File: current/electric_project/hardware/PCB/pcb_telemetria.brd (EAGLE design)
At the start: 106.8 x 113.8 mm, 42 parts

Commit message: Schematic e code conforming
The mux pins in the code are now updated (EN on the ground rsrs) and the circuit project are already routed with the new mux pins
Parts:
- moved SUPPLY 6.87 mm to (96.6, 77.9)
- moved SHUNTS 6.60 mm to (96.3, 96.6)
- moved TEMP2 6.13 mm to (96.3, 85.4)
- moved TEMP1 5.98 mm to (96.4, 90.9)
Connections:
- removed net GND1: U$1.GND1
- net 13: now also HC4067.J2.6
- net 14: now also HC4067.J2.5
- net 33: no longer HC4067.J2.3
- net 34: no longer HC4067.J2.6
- net 35: no longer HC4067.J2.5
- net GND: now also HC4067.J2.3, U$1.GND1
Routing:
- net 14: track 0.00 -> 130.9 mm
- net 33: track 118.8 -> 0.00 mm
- net 13: track 0.00 -> 114.1 mm
- net 35: track 111.4 -> 0.00 mm
- net 34: track 106.1 -> 0.00 mm
- net 32: track 115.3 -> 150.3 mm
- net VCC: track 233.7 -> 255.4 mm
- net VI: track 15.2 -> 11.5 mm
- net 21: track 74.5 -> 73.0 mm
- net 22: track 58.3 -> 58.9 mm
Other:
- board size 106.8 x 113.8 mm -> 106.8 x 120.2 mm

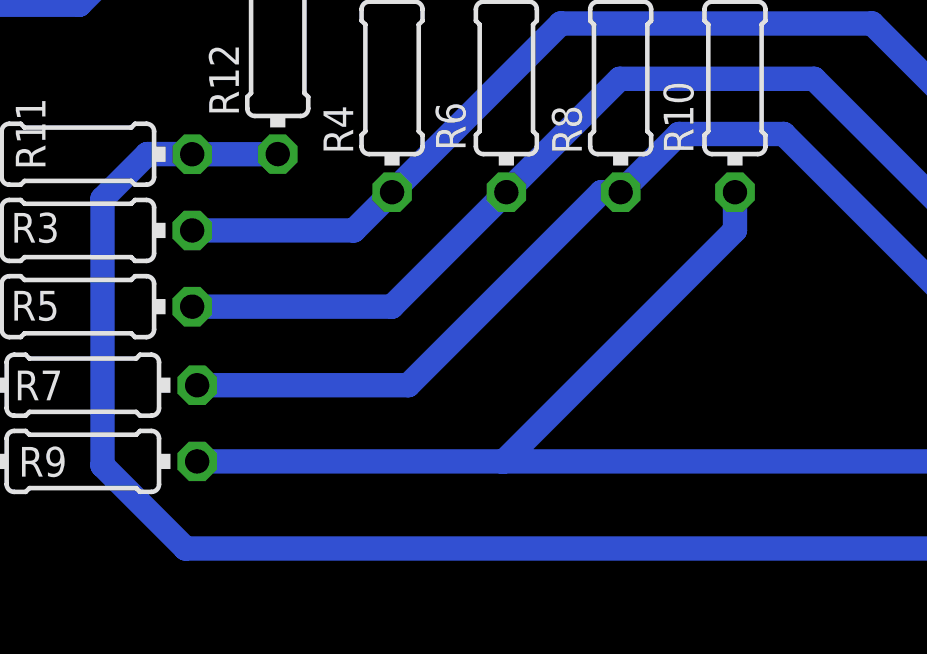
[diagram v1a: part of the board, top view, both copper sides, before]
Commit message: mudancas na placa
resistores atualizados com sucesso

Co-Authored-By: Raquel Perim <raquelperim@users.noreply.github.com>
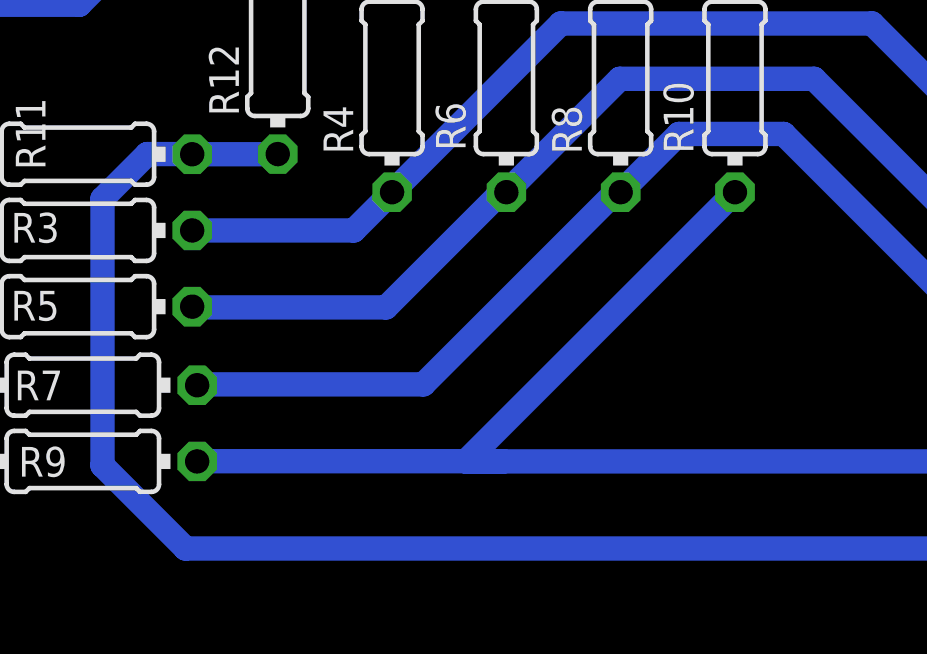
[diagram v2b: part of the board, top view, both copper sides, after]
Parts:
- R1: value 100k -> 330k
- R11: value 2.2k -> 220k
- R12: value 3.9k -> 390k
- R15, R17, R19, R21, R23: value 220k -> 270k
- R16, R18, R20, R22, R24: value 62k -> 68k
- R2: value 3.9k -> 12k
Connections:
- removed net BTN_CRUZEIRO: R9.2, SL7.2
- removed net COOLER_D: R19.1, SL3.2
- removed net ON-OFF_MOTOR: R7.1, SL7.1
- new net BTN_CRUZ: R3.1, SL2.2
- new net BTN_M: R5.2, SL2.3
- new net COOLER_B: R23.1, SL4.3
- net BTN_RE: now also R7.1, SL7.1; no longer R5.2, SL2.3
- net COOLER_E: now also R19.1, SL3.2; no longer R23.1, SL4.3
- net DMS_IN: now also R9.2, SL7.2; no longer R3.1, SL2.2
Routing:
- net ON-OFF_MOTOR: track 14.5 -> 0.00 mm
- net BTN_CRUZEIRO: track 14.5 -> 0.00 mm
- net BTN_M: track 0.00 -> 14.3 mm
- net BTN_CRUZ: track 0.00 -> 14.3 mm
- net COOLER_D: track 5.53 -> 0.00 mm
- net COOLER_B: track 0.00 -> 5.00 mm
- net C0: track 45.4 -> 47.1 mm
- net COOLER_E: track 5.00 -> 5.53 mm
